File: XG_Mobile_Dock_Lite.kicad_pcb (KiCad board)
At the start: 4 copper layers, 220 x 65 mm, 58 parts, among them J1 5-1775443-8, J10 SWD, J11 UART, J12 I2C1, J13 39300240, J14 469911008, J17 8730, J2 20455-040E-76, J20 8730, J3 20455-040E-76, J4 3-2362375-4, J5 USB_C_Receptacle, Q16 AO3401A, Q17 2N7002W, SW1 SW_Push, U12 STM32F030C8Tx

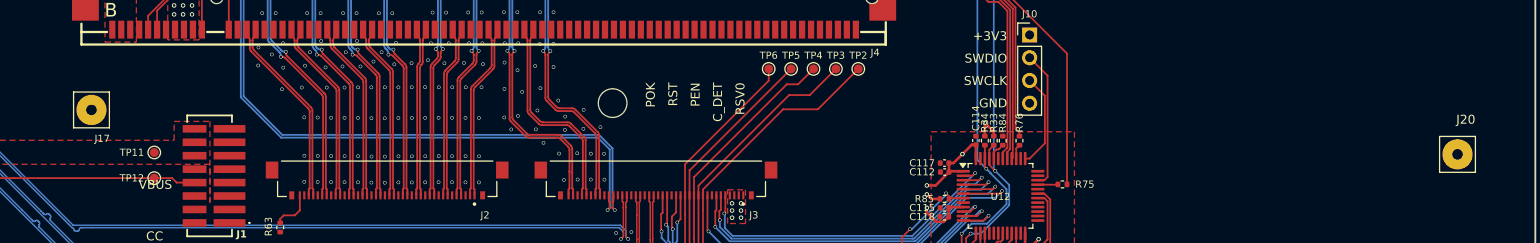
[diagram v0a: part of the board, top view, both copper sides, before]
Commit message: added better ground screw
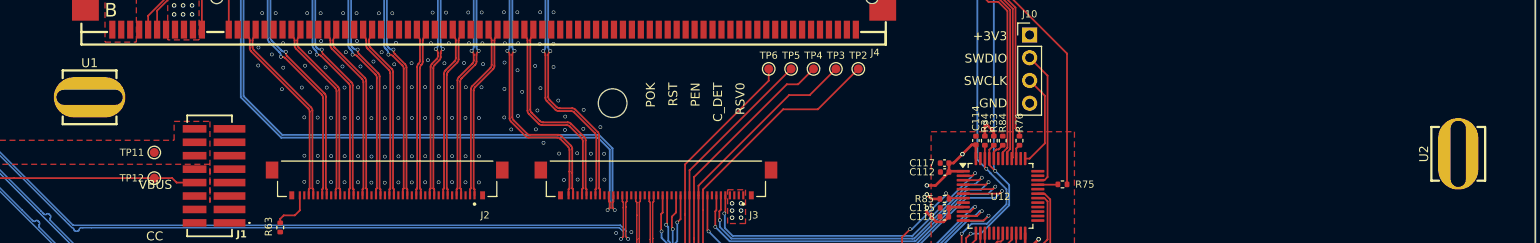
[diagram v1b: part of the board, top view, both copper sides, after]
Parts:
- removed J17, J20: 8730, KEYSTONE_8730:KEYSTONE_8730
- added U1: ~, CONN-SMD_T31000:CONN-SMD_T31000, F.Cu at (75.4, 71.3)
- added U2: ~, CONN-SMD_T31000:CONN-SMD_T31000, F.Cu at (228.2, 77.6)

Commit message: fixed more issues
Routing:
- net GND: vias 162 -> 165
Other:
- board text added: "XG Mobile Dock Lite v0.7"
- board text removed: "XG Mobile Dock Lite v0.6"
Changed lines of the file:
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@@
 		)
 	)
-	(gr_text "XG Mobile Dock Lite v0.6"
+	(gr_text "XG Mobile Dock Lite v0.7"
 		(at 75.621496 55.121496 0)
 		(layer "F.SilkS")
@@
 	)
 	(via
-		(at 135.5 89)
+		(at 135.65 87.96)
 		(size 0.4)
 		(drill 0.3)
@@
 	)
 	(via
+		(at 137.45 87.83)
+		(size 0.4)
+		(drill 0.3)
+		(layers "F.Cu" "B.Cu")
+		(free yes)
+		(net 1)
+	)
+	(via
 		(at 115.01 67.48)
 		(size 0.4)
@@
 	(via
 		(at 128.49 73.43)
+		(size 0.4)
+		(drill 0.3)
+		(layers "F.Cu" "B.Cu")
+		(free yes)
+		(net 1)
+	)
+	(via
+		(at 132.89 84.54)
 		(size 0.4)
 		(drill 0.3)
@@
 	)
 	(via
-		(at 135.88 86.32)
+		(at 135.86 86.37)
 		(size 0.4)
 		(drill 0.3)
@@
 		(size 0.4)
 		(drill 0.3)
+		(layers "F.Cu" "B.Cu")
+		(free yes)
+		(net 1)
+	)
+	(via
+		(at 134.29 84.57)
+		(size 0.4)
+		(drill 0.3)
